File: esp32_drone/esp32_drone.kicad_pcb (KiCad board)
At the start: 2 copper layers, 31.1 x 28.7 mm, 33 parts, among them J1 Conn_01x07_Socket, J2 Conn_01x07_Socket, J3 B2B-PH-K-S_LF__SN_, M1 Motor_DC, M2 Motor_DC, M3 Motor_DC, M4 Motor_DC, Q2 IRLML2502TRPBF, Q3 IRLML2502TRPBF, Q4 IRLML2502TRPBF, Q5 IRLML2502TRPBF

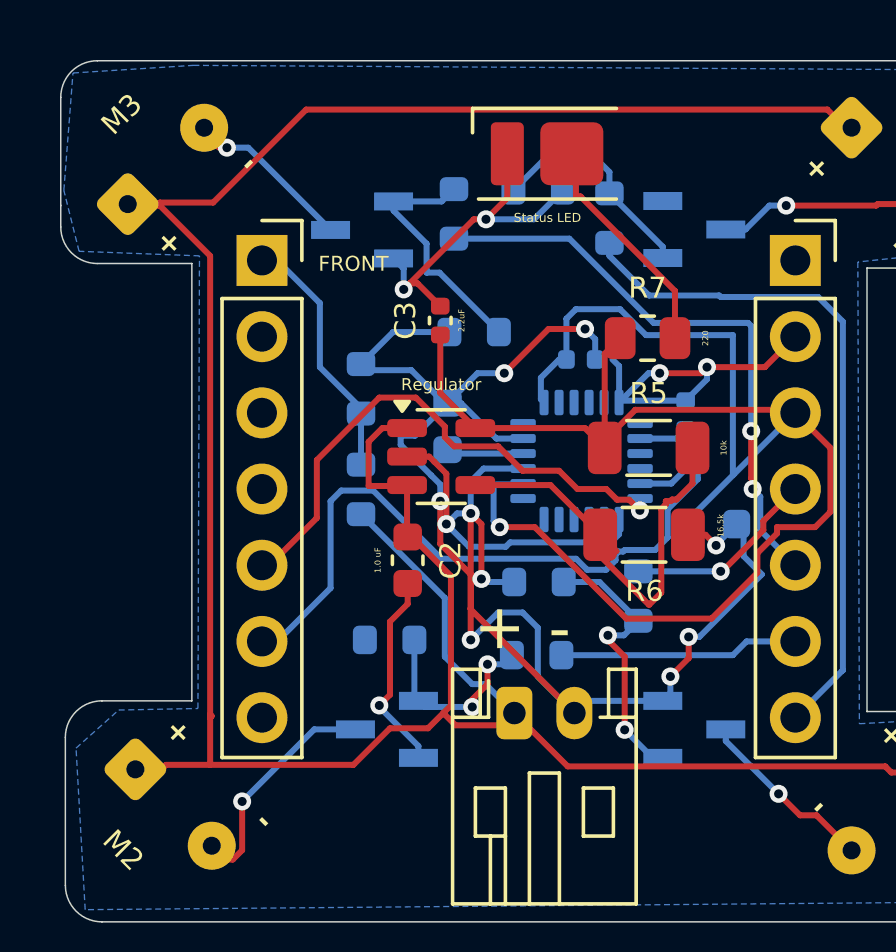
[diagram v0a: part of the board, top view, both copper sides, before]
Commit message: reduced ground vias
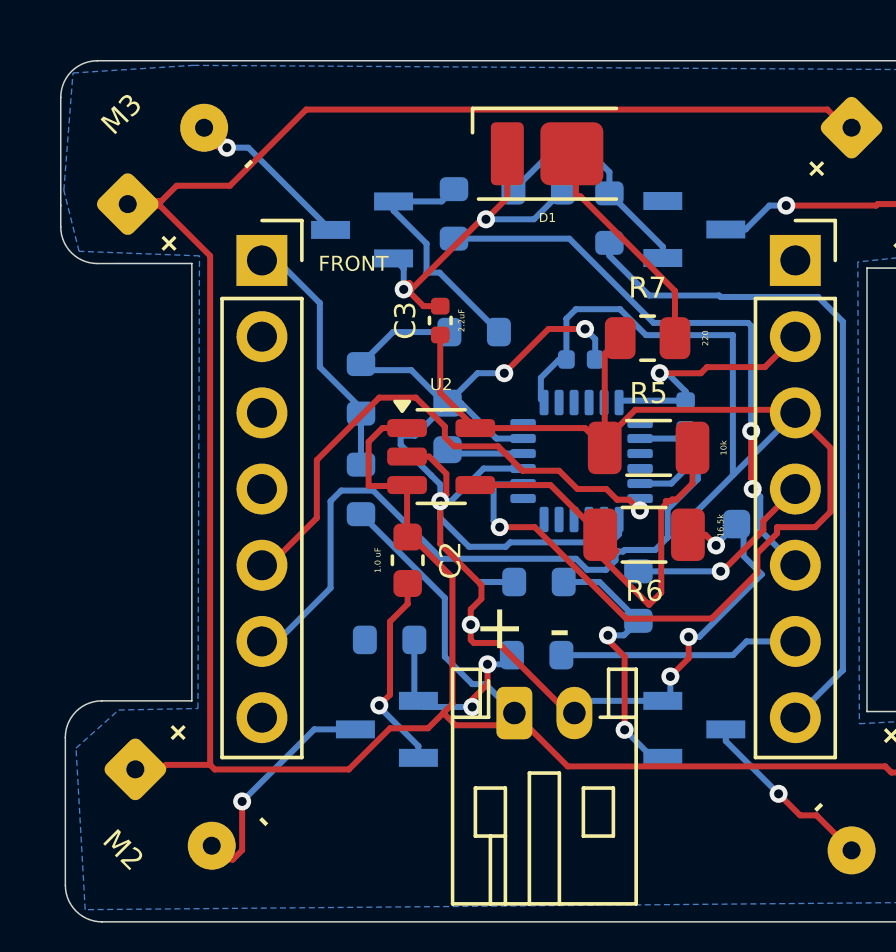
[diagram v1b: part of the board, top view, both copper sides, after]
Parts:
- D1: renamed from Status LED
- renumbered MPU6050 to U1, Regulator to U2
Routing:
- net GND: track 101.8 -> 86.8 mm, vias 15 -> 11

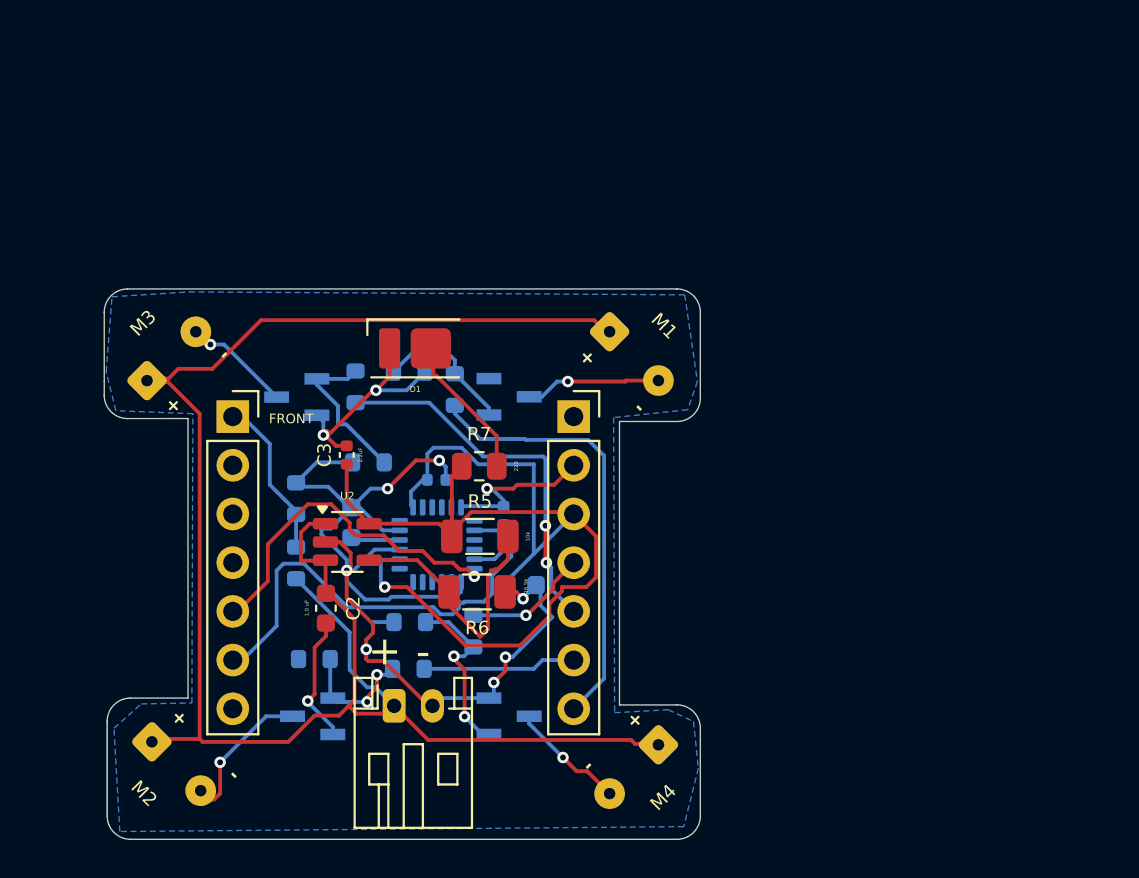
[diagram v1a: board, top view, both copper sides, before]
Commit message: finished without flyback diode
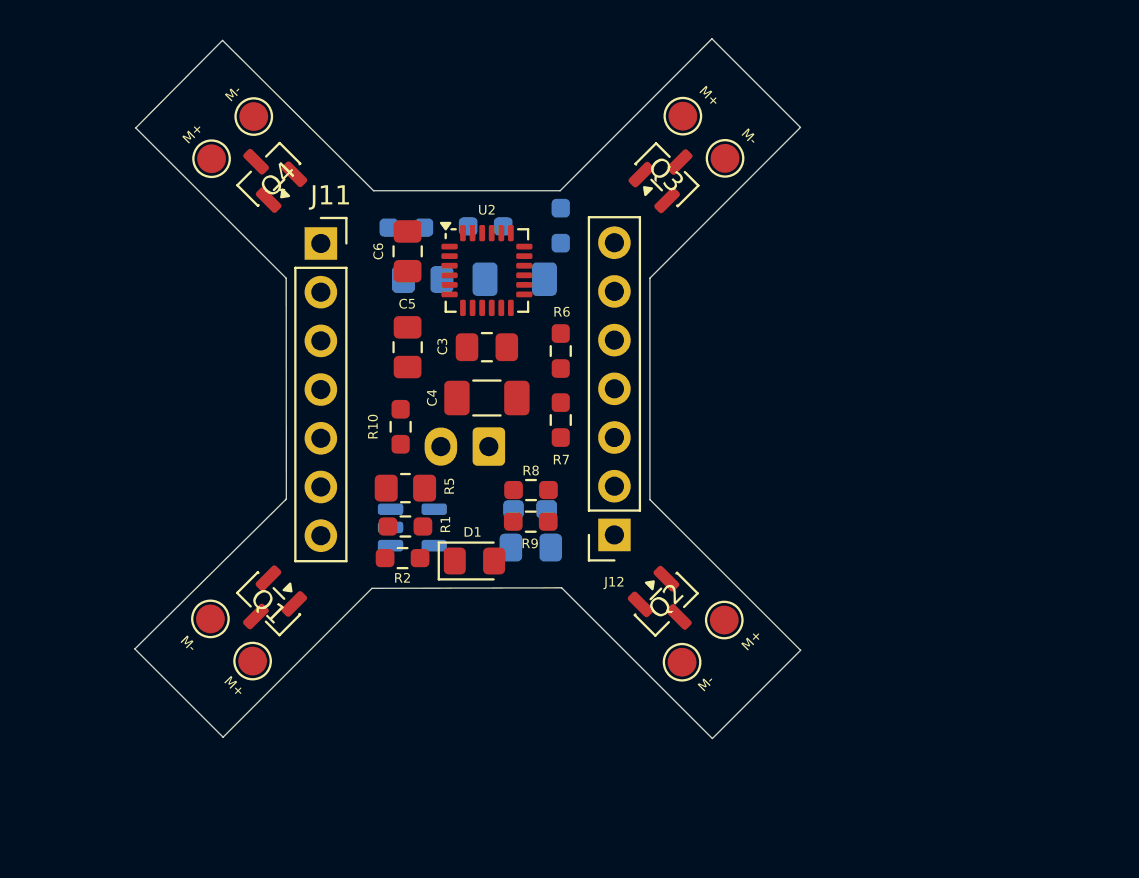
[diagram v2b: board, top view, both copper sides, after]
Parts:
- removed M1, M2, M3, M4: Motor_DC, Connector_Wire:SolderWire-0.1sqmm_1x02_P3.6mm_D0.4mm_OD1mm
- removed Q5: IRLML2502TRPBF, digikey-footprints:SOT-23-3
- removed R14: 100, Resistor_SMD:R_0603_1608Metric
- removed R15: 100k, Resistor_SMD:R_0603_1608Metric
- added G***: LOGO, LOGO, B.Cu at (111.7, 88.0)
- added J11: EE_SOCKET_01x07, Connector_PinSocket_2.54mm:PinSocket_1x07_P2.54mm_Vertical, F.Cu at (115.5, 68.3)
- added J12: EE_SOCKET_01x07, Connector_PinSocket_2.54mm:PinSocket_1x07_P2.54mm_Vertical, F.Cu at (130.8, 83.5)
- added J4: EE_SOCKET_01x01, TestPoint:TestPoint_Pad_D1.5mm, F.Cu at (134.3, 90.2)
- added J5: EE_SOCKET_01x01, TestPoint:TestPoint_Pad_D1.5mm, F.Cu at (134.4, 61.7)
- added J6: EE_SOCKET_01x01, TestPoint:TestPoint_Pad_D1.5mm, F.Cu at (136.6, 63.9)
- added J7: EE_SOCKET_01x01, TestPoint:TestPoint_Pad_D1.5mm, F.Cu at (109.8, 63.9)
- added J8: EE_SOCKET_01x01, TestPoint:TestPoint_Pad_D1.5mm, F.Cu at (112.0, 61.7)
- added J9: Conn_01x02_Pin, Connector_JST:JST_EH_S2B-EH_1x02_P2.50mm_Horizontal, B.Cu at (124.2, 78.9)
- added Q1: AO3400A, Package_TO_SOT_SMD:SOT-23, F.Cu at (112.8, 87.1)
- added R1: 100K, Resistor_SMD:R_0603_1608Metric_Pad0.98x0.95mm_HandSolder, F.Cu at (119.9, 83.1)
- added R2: 100, Resistor_SMD:R_0603_1608Metric_Pad0.98x0.95mm_HandSolder, F.Cu at (119.8, 84.8)
- C1: value 2.2nF -> 0.1uF; footprint Capacitor_SMD:C_0402_1005Metric -> Capacitor_SMD:C_0805_2012Metric_Pad1.18x1.45mm_HandSolder
- C2: value 1.0 uF -> 2.2uF; footprint Capacitor_SMD:C_0603_1608Metric -> Capacitor_SMD:C_0603_1608Metric_Pad1.08x0.95mm_HandSolder; moved to B.Cu
- C3: value 2.2uF -> 0.1uF; footprint Capacitor_SMD:C_0402_1005Metric -> Capacitor_SMD:C_0805_2012Metric_Pad1.18x1.45mm_HandSolder
- C4: value 0.1uF -> 10nF; footprint Capacitor_SMD:C_0603_1608Metric -> Capacitor_SMD:C_1206_3216Metric_Pad1.33x1.80mm_HandSolder; moved to F.Cu
- C5: footprint Capacitor_SMD:C_0603_1608Metric -> Capacitor_SMD:C_0805_2012Metric_Pad1.18x1.45mm_HandSolder; moved to F.Cu
- C6: value 10nF -> 2.2nF; footprint Capacitor_SMD:C_0402_1005Metric -> Capacitor_SMD:C_0805_2012Metric_Pad1.18x1.45mm_HandSolder; moved to F.Cu
- D1: footprint LED_SMD:LED_Everlight-SMD3528_3.5x2.8mm_67-21ST -> LED_SMD:LED_0805_2012Metric_Pad1.15x1.40mm_HandSolder
- J1, J2: value Conn_01x07_Socket -> EE_SOCKET_01x01; footprint Connector_PinSocket_2.54mm:PinSocket_1x07_P2.54mm_Vertical -> TestPoint:TestPoint_Pad_D1.5mm
- J3: value B2B-PH-K-S_LF__SN_ -> EE_SOCKET_01x01; footprint Connector_JST:JST_PH_S2B-PH-K_1x02_P2.00mm_Horizontal -> TestPoint:TestPoint_Pad_D1.5mm
- Q2, Q3, Q4: value IRLML2502TRPBF -> AO3400A; footprint digikey-footprints:SOT-23-3 -> Package_TO_SOT_SMD:SOT-23; moved to F.Cu
- R10, R8: footprint Resistor_SMD:R_0603_1608Metric -> Resistor_SMD:R_0603_1608Metric_Pad0.98x0.95mm_HandSolder; moved to F.Cu
- R11, R13: value 100k -> 100K; footprint Resistor_SMD:R_0603_1608Metric -> Resistor_SMD:R_0603_1608Metric_Pad0.98x0.95mm_HandSolder
- R12: footprint Resistor_SMD:R_0603_1608Metric -> Resistor_SMD:R_0603_1608Metric_Pad0.98x0.95mm_HandSolder
- R3: value 100k -> 10k; footprint Resistor_SMD:R_0603_1608Metric -> Resistor_SMD:R_0805_2012Metric_Pad1.20x1.40mm_HandSolder
- R4: value 100k -> 16.5k; footprint Resistor_SMD:R_0603_1608Metric -> Resistor_SMD:R_1206_3216Metric_Pad1.30x1.75mm_HandSolder
- R5: value 10k -> 220; footprint Resistor_SMD:R_1206_3216Metric -> Resistor_SMD:R_0805_2012Metric_Pad1.20x1.40mm_HandSolder
- R6: value 16.5k -> 100K; footprint Resistor_SMD:R_1206_3216Metric -> Resistor_SMD:R_0603_1608Metric_Pad0.98x0.95mm_HandSolder
- R7: value 220 -> 100K; footprint Resistor_SMD:R_0805_2012Metric -> Resistor_SMD:R_0603_1608Metric_Pad0.98x0.95mm_HandSolder
- R9: value 100k -> 100K; footprint Resistor_SMD:R_0603_1608Metric -> Resistor_SMD:R_0603_1608Metric_Pad0.98x0.95mm_HandSolder; moved to F.Cu
- U1: value MPU-6050 -> AP2204K-ADJ; footprint Sensor_Motion:InvenSense_QFN-24_4x4mm_P0.5mm -> Package_TO_SOT_SMD:SOT-23-5
- U2: value AP2204K-ADJ -> MPU-6050; footprint Package_TO_SOT_SMD:SOT-23-5 -> Sensor_Motion:InvenSense_QFN-24_4x4mm_P0.5mm
- moved Q3 33.8 mm to (133.5, 64.8), turned to 45 degrees
- moved R11 26.0 mm to (128.0, 67.4), turned to 90 degrees
- moved J1 21.0 mm to (111.9, 90.1), turned to 45 degrees
- moved J3 17.8 mm to (136.5, 88.0), turned to 45 degrees
- moved R3 16.2 mm to (120.8, 70.2), turned to 180 degrees
- moved R4 16.2 mm to (125.6, 70.2), turned to 0 degrees
- moved U2 15.9 mm to (124.2, 69.8)
- moved C5 13.8 mm to (120.0, 73.8), turned to -90 degrees
- moved Q2 13.6 mm to (133.5, 87.2), turned to -45 degrees
- moved R6 13.3 mm to (128.0, 74.0), turned to 90 degrees
- moved R10 12.6 mm to (119.7, 77.9), turned to 90 degrees
- moved R13 12.4 mm to (120.0, 67.5), turned to 180 degrees
- moved C6 12.0 mm to (120.0, 68.8), turned to 90 degrees
- moved C2 11.8 mm to (126.4, 82.2), turned to 0 degrees
- moved Q4 11.7 mm to (112.8, 64.7), turned to 135 degrees
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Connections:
- C1 pad 1: Net-(U1-CPOUT) -> VCC
- C2 pad 1: /3.7V -> /3V3
- C4 pad 1: Net-(U1-REGOUT) -> /3V3
- C5 pad 1: /3V3 -> GND
- C5 pad 2: GND -> Net-(U2-REGOUT)
- C6 pad 1: /3V3 -> GND
- C6 pad 2: GND -> Net-(U2-CPOUT)
- J1 pad 1: unconnected-(J1-Pin_1-Pad1) -> VCC
- J2 pad 1: /A0 -> /MOTOR1_-
- J3 pad 1: /3.7V -> VCC
- Q2 pad 3: Net-(M1--) -> /MOTOR2_-
- Q3 pad 3: Net-(M2--) -> /MOTOR3_-
- Q4 pad 3: Net-(M3--) -> /MOTOR4_-
- R10 pad 1: /PWM2 -> /PWM3
- R11 pad 1: GND -> Net-(Q3-G)
- R11 pad 2: Net-(Q3-G) -> GND
- R12 pad 1: /PWM3 -> /PWM4
- R13 pad 1: GND -> Net-(Q4-G)
- R13 pad 2: Net-(Q4-G) -> GND
- R3 pad 1: /A0 -> /3V3
- R3 pad 2: /3.7V -> Net-(U1-ADJ)
- R4 pad 1: GND -> Net-(U1-ADJ)
- R4 pad 2: /A0 -> GND
- R5 pad 2: Net-(U2-ADJ) -> Net-(D1-A)
- R6 pad 1: Net-(U2-ADJ) -> /A0
- R6 pad 2: GND -> VCC
- R7 pad 1: Net-(D1-A) -> GND
- R7 pad 2: /3V3 -> /A0
- R8 pad 1: /PWM1 -> /PWM2
- R9 pad 1: GND -> Net-(Q2-G)
- R9 pad 2: Net-(Q2-G) -> GND
- U1 pad 1: GND -> VCC
- U1 pad 2: unconnected-(U1-NC-Pad2) -> GND
- U1 pad 3: unconnected-(U1-NC-Pad3) -> VCC
- U1 pad 4: unconnected-(U1-NC-Pad4) -> Net-(U1-ADJ)
- U1 pad 5: unconnected-(U1-NC-Pad5) -> /3V3
- U2 pad 1: /3.7V -> GND
- U2 pad 2: GND -> unconnected-(U2-NC-Pad2)
- U2 pad 3: /3.7V -> unconnected-(U2-NC-Pad3)
- U2 pad 4: Net-(U2-ADJ) -> unconnected-(U2-NC-Pad4)
- U2 pad 5: /3V3 -> unconnected-(U2-NC-Pad5)
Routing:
- net /3.7V: track 96.5 -> 0.00 mm
- net GND: track 86.8 -> 0.00 mm, vias 11 -> 0
- net /3V3: track 58.9 -> 0.00 mm, vias 1 -> 0
- net /SCL: track 24.4 -> 0.00 mm
- net /PWM1: track 23.0 -> 0.00 mm
- net /PWM3: track 19.9 -> 0.00 mm, vias 2 -> 0
- net /SDA: track 18.2 -> 0.00 mm, vias 1 -> 0
- net Net-(U2-ADJ): track 14.6 -> 0.00 mm
- net Net-(Q5-G): track 9.28 -> 0.00 mm, vias 2 -> 0
- net /A0: track 8.47 -> 0.00 mm
- net Net-(Q4-G): track 8.25 -> 0.00 mm
- net /PWM2: track 7.99 -> 0.00 mm
- net Net-(D1-A): track 7.66 -> 0.00 mm
- net Net-(Q2-G): track 7.52 -> 0.00 mm
- net Net-(M1--): track 7.23 -> 0.00 mm, vias 1 -> 0
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- removed copper zone on B.Cu, net GND
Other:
- board size 31.1 x 28.7 mm -> 34.7 x 36.5 mm
- board text added: "M+"
- board text added: "M-"
- board text removed: "+"
- board text removed: "-"
- board text removed: "Emir Kılıçaslan"
- board text removed: "FRONT"
- board text removed: "https://github.com/cronuxx/esp32_drone"

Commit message: finished routing
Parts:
- added D2: UF4007, Diode_SMD:D_SOD-323_HandSoldering, F.Cu at (111.2, 81.2)
- added D3: UF4007, Diode_SMD:D_SOD-323_HandSoldering, F.Cu at (116.5, 62.0)
- added D4: UF4007, Diode_SMD:D_SOD-323_HandSoldering, F.Cu at (137.2, 82.3)
- added D5: UF4007, Diode_SMD:D_SOD-323_HandSoldering, F.Cu at (134.7, 68.3)
- G***: moved to F.Cu
- moved R12 14.1 mm to (119.0, 80.6), turned to 0 degrees
- moved R11 13.7 mm to (119.0, 77.8), turned to 180 degrees
- moved R4 11.6 mm to (123.0, 81.5), turned to -90 degrees
- moved G*** 11.0 mm to (122.7, 88.0), turned to 0 degrees
- moved C2 9.53 mm to (119.0, 76.2), turned to 180 degrees
- moved R13 8.76 mm to (128.7, 67.9), turned to 90 degrees
- moved C1 8.06 mm to (127.4, 76.2)
- moved R3 7.79 mm to (128.5, 71.5), turned to 90 degrees
- moved U1 6.75 mm to (123.1, 77.0), turned to 180 degrees
- moved J9 6.08 mm to (124.0, 72.9)
- moved C3 6.06 mm to (118.4, 71.8), turned to 90 degrees
- moved C5 5.89 mm to (119.5, 67.9)
- moved Q2 4.94 mm to (134.5, 82.3), turned to -90 degrees
- moved R8 3.88 mm to (124.0, 78.2)
- moved Q4 3.64 mm to (116.4, 64.7), turned to 180 degrees
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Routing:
- net VCC: track 0.00 -> 86.4 mm, vias 0 -> 8
- net Net-(Q4-G): track 0.00 -> 50.4 mm, vias 0 -> 1
- net /3V3: track 0.00 -> 42.3 mm, vias 0 -> 1
- net GND: track 0.00 -> 40.3 mm, vias 0 -> 21
- net Net-(Q3-G): track 0.00 -> 33.8 mm, vias 0 -> 4
- net /PWM1: track 0.00 -> 20.0 mm
- net /SDA: track 0.00 -> 17.9 mm
- net Net-(Q1-G): track 0.00 -> 16.1 mm
- net /PWM2: track 0.00 -> 15.8 mm, vias 0 -> 2
- net Net-(Q2-G): track 0.00 -> 15.7 mm, vias 0 -> 2
- net Net-(U1-ADJ): track 0.00 -> 13.1 mm
- net /SCL: track 0.00 -> 12.6 mm
- net Net-(D1-A): track 0.00 -> 11.6 mm, vias 0 -> 2
- net Net-(U2-REGOUT): track 0.00 -> 10.2 mm, vias 0 -> 2
- net /A0: track 0.00 -> 9.86 mm
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- added copper zone on B.Cu, net GND
- added copper zone on In1.Cu, net GND
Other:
- board size 34.7 x 36.5 mm -> 30.4 x 30.4 mm
- copper layers 2 -> 4

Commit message: finished last product
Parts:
- J1, J2, J3, J4, J5, J6, J7, J8: footprint TestPoint:TestPoint_Pad_D1.5mm -> TestPoint:TestPoint_THTPad_D2.0mm_Drill1.0mm
- J9, R13: moved to F.Cu
- moved G*** 17.7 mm to (135.4, 75.6)
- moved D1 15.4 mm to (112.4, 73.3), turned to -90 degrees
- moved R10 14.1 mm to (127.0, 63.6), turned to 0 degrees
- moved R2 10.9 mm to (111.8, 76.5)
- moved J9 10.8 mm to (124.3, 83.6)
- moved R12 10.6 mm to (119.2, 70.0), turned to 90 degrees
- moved R13 10.3 mm to (118.4, 68.1), turned to -90 degrees
- moved R6 9.20 mm to (128.2, 83.2), turned to -90 degrees
- moved R4 8.62 mm to (121.0, 73.2), turned to 180 degrees
- moved R1 7.54 mm to (111.8, 78.2)
- moved C1 6.62 mm to (121.7, 79.6), turned to 180 degrees
- moved U1 4.54 mm to (127.0, 79.3), turned to 0 degrees
- moved C5 4.28 mm to (121.3, 71.8), turned to 0 degrees
- moved C2 2.43 mm to (121.3, 75.6), turned to 0 degrees
- moved R9 2.43 mm to (123.9, 77.8)
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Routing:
- net Net-(Q4-G): track 50.4 -> 7.11 mm
- net GND: track 40.3 -> 71.2 mm, vias 21 -> 16
- net /3V3: track 42.3 -> 57.6 mm, vias 1 -> 7
- net Net-(Q3-G): track 33.8 -> 18.8 mm, vias 4 -> 1
- net Net-(U2-CPOUT): track 6.38 -> 21.2 mm
- net /PWM3: track 5.27 -> 19.0 mm
- net /PWM1: track 20.0 -> 9.32 mm
- net /PWM2: track 15.8 -> 10.3 mm, vias 2 -> 0
- net /A0: track 9.86 -> 4.84 mm
- net Net-(U2-REGOUT): track 10.2 -> 15.0 mm, vias 2 -> 0
- net Net-(Q1-G): track 16.1 -> 11.4 mm, vias 0 -> 2
- net /SDA: track 17.9 -> 13.6 mm
- net /SCL: track 12.6 -> 8.84 mm
- net Net-(Q2-G): track 15.7 -> 18.6 mm, vias 2 -> 0
- net Net-(U1-ADJ): track 13.1 -> 10.2 mm
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- added copper zone on F.Cu, net GND

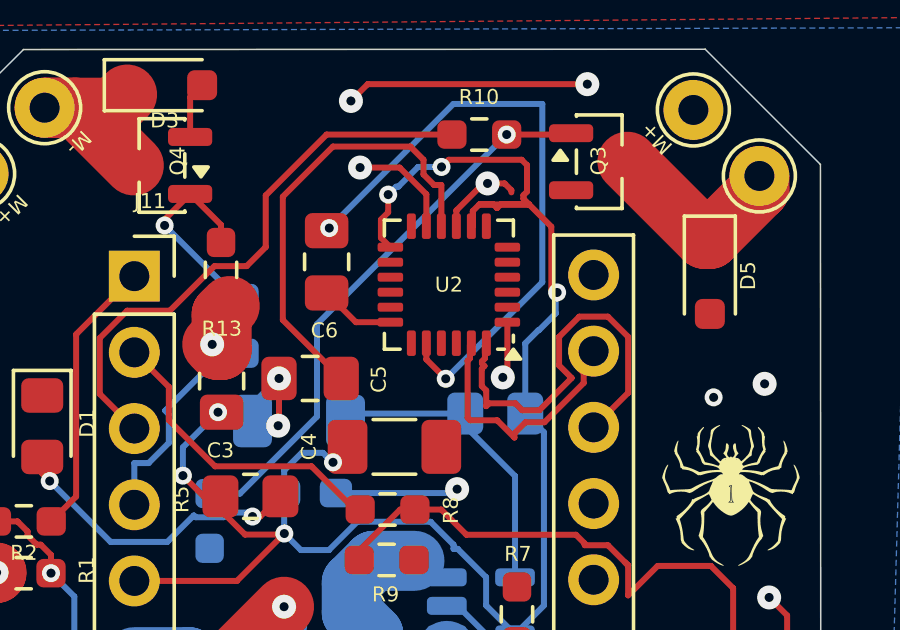
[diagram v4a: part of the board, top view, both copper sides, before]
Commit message: updated mpu6050 footprint
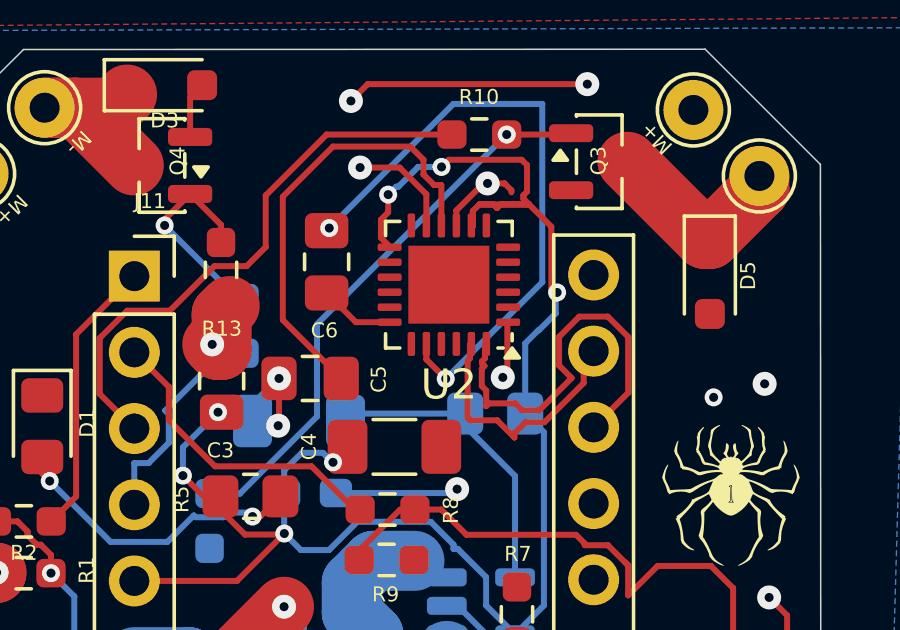
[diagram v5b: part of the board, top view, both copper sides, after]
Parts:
- U2: footprint Sensor_Motion:InvenSense_QFN-24_4x4mm_P0.5mm -> Package_DFN_QFN:QFN-24-1EP_4x4mm_P0.5mm_EP2.7x2.6mm
